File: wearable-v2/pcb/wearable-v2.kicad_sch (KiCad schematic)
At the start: 0 parts

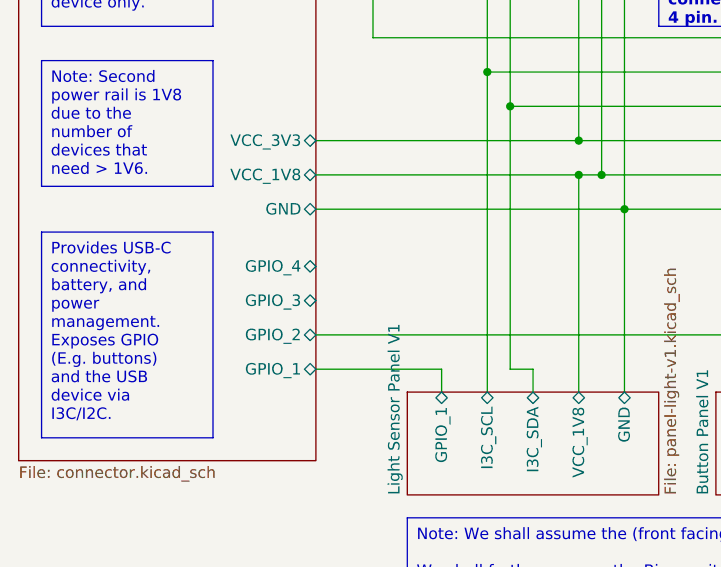
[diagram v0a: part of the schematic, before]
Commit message: Updated components and PCB layout
Signed-off-by: Adam Fowler <adam@adamfowler.org>
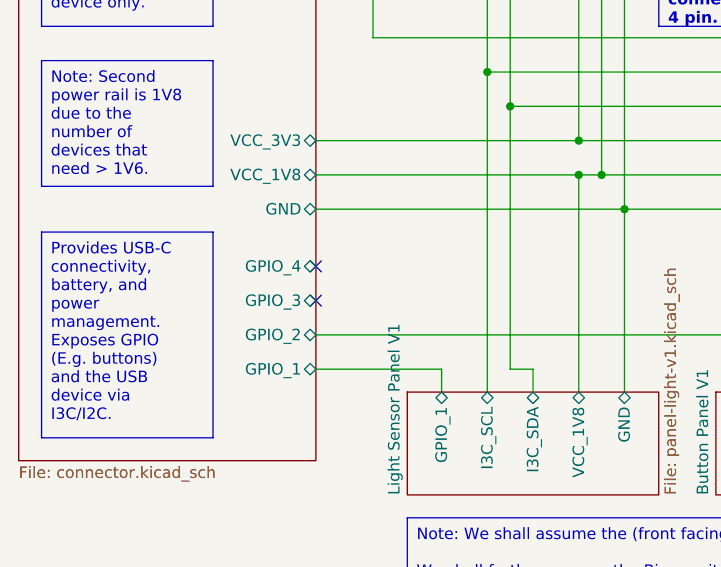
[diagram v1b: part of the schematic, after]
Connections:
- no-connect marks 0 -> 2
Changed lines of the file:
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@@
   (junction (at 87.63 93.98) (diameter 0) (color 0 0 0 0)
   )
+  (no_connect (at 58.42 142.24))
+  (no_connect (at 58.42 138.43))
   (wire (pts (xy 90.17 67.31) (xy 90.17 97.79))
     (stroke (width 0) (type default))

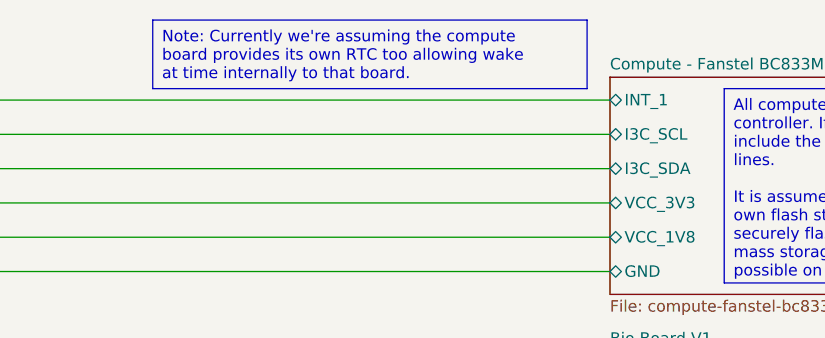
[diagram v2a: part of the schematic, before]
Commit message: Added front connectors on main board
Signed-off-by: Adam Fowler <adam@adamfowler.org>
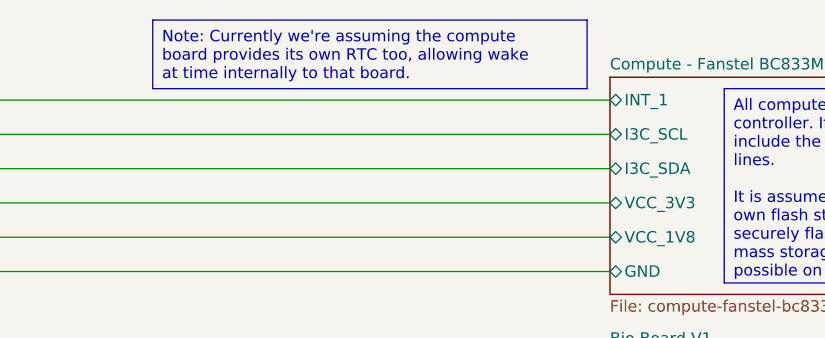
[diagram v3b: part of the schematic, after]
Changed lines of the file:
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@@
     (effects (font (size 1.27 1.27)) (justify left top))
   )
-  (text_box "Note: Currently we're assuming the compute board provides its own RTC too allowing wake at time internally to that board."
+  (text_box "Note: Currently we're assuming the compute board provides its own RTC too, allowing wake at time internally to that board."
     (at 170.18 12.7 0) (size 48.26 7.62)
     (stroke (width 0) (type default))

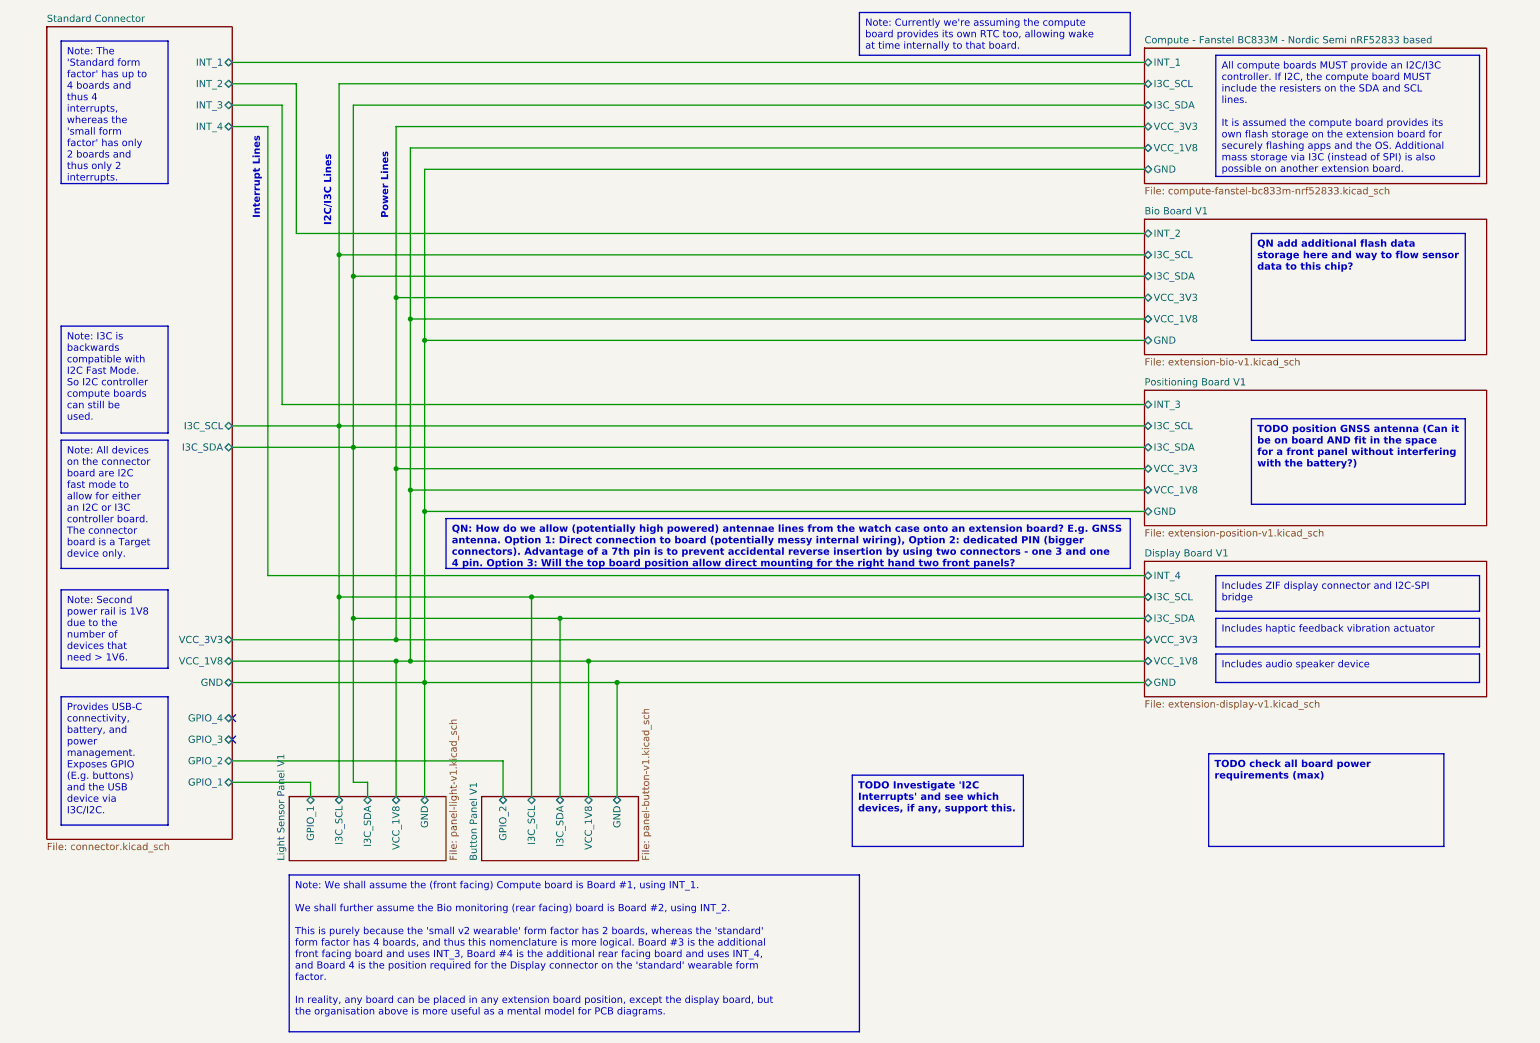
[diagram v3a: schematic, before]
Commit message: Added I2C and I3C notes and additional resistors
Signed-off-by: Adam Fowler <adam@adamfowler.org>
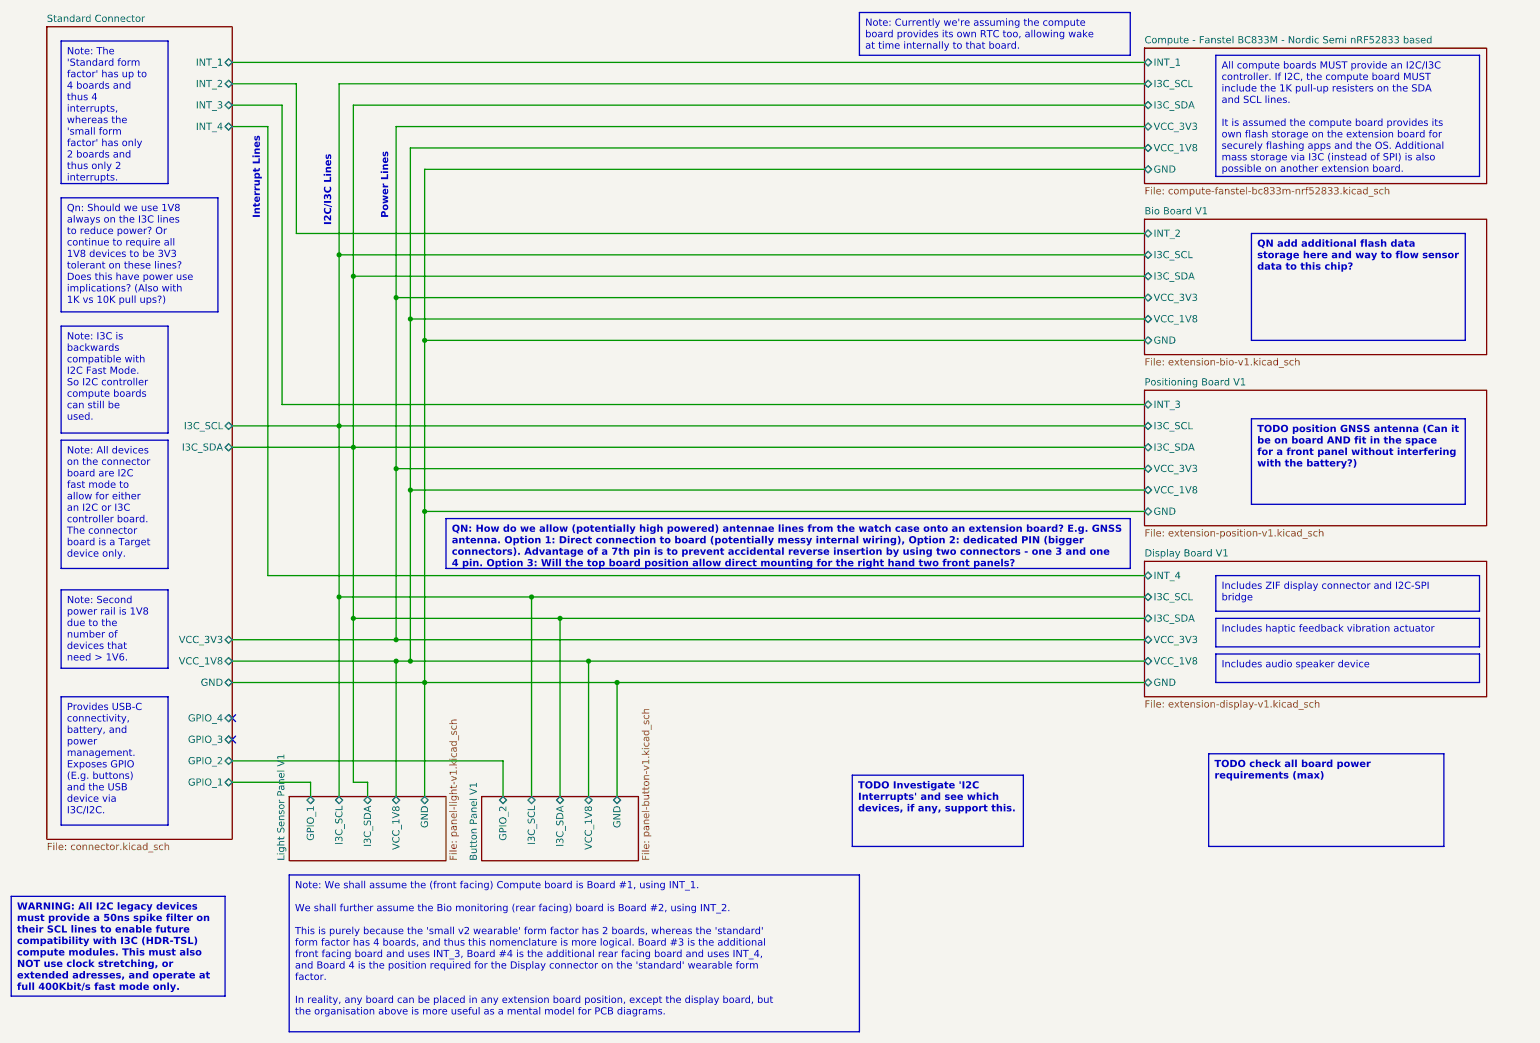
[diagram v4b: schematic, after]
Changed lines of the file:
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@@
     (stroke (width 0) (type default))
+  )
+  (text_box "Qn: Should we use 1V8 always on the I3C lines to reduce power? Or continue to require all 1V8 devices to be 3V3 tolerant on these lines? Does this have power use implications? (Also with 1K vs 10K pull ups?)"
+    (at 27.94 45.72 0) (size 27.94 20.32)
+    (stroke (width 0) (type default))
+    (fill (type none))
+    (effects (font (size 1.27 1.27)) (justify left top))
   )
   (text_box "Includes haptic feedback vibration actuator"
@@
     (fill (type none))
     (effects (font (size 1.27 1.27)) (justify left top))
+  )
+  (text_box "WARNING: All I2C legacy devices must provide a 50ns spike filter on their SCL lines to enable future compatibility with I3C (HDR-TSL) compute modules. This must also NOT use clock stretching, or extended adresses, and operate at full 400Kbit/s fast mode only."
+    (at 19.05 170.18 0) (size 38.1 17.78)
+    (stroke (width 0) (type default))
+    (fill (type none))
+    (effects (font (size 1.27 1.27) (thickness 0.254) bold) (justify left top))
   )
   (text_box "Provides USB-C connectivity, battery, and power management. Exposes GPIO (E.g. buttons) and the USB device via I3C/I2C."
@@
     (effects (font (size 1.27 1.27)) (justify left top))
   )
-  (text_box "All compute boards MUST provide an I2C/I3C controller. If I2C, the compute board MUST include the resisters on the SDA and SCL lines.\n\nIt is assumed the compute board provides its own flash storage on the extension board for securely flashing apps and the OS. Additional mass storage via I3C (instead of SPI) is also possible on another extension board."
+  (text_box "All compute boards MUST provide an I2C/I3C controller. If I2C, the compute board MUST include the 1K pull-up resisters on the SDA and SCL lines.\n\nIt is assumed the compute board provides its own flash storage on the extension board for securely flashing apps and the OS. Additional mass storage via I3C (instead of SPI) is also possible on another extension board."
     (at 233.68 20.32 0) (size 46.99 21.59)
     (stroke (width 0) (type default))
